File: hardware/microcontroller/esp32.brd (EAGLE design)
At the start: 108 x 93.9 mm, 20 parts, among them IC1 ESP32-WROOM-32U, IC2 AMS1117-1.5

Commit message: ESP32 Schematic clean-up
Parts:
- removed J3: (no value), con-amp:10X06MTA
- added UPLOAD_PROGRAMME: (no value), con-amp:1X6MTA
- GSM: device con-amp:1X4MTA -> con-amp:1X5MTA
- RFID: device con-amp:10X08MTA -> con-amp:1X8MTA
- moved GSM 81.0 mm to (-12.7, -34.3), turned to 0 degrees
- moved RFID 34.3 mm to (-6.35, -19.1), turned to 0 degrees
- moved POWER 17.0 mm to (74.9, 9.62)
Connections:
- new net GSM_VCC: GSM.5, GSM_VCC.1
- net GND: now also GSM.4, UPLOAD_PROGRAMME.6; no longer GSM.3, J3.6
- net GSM_RESET: now also GSM.3; no longer GSM.4, GSM_VCC.1
- net RX: now also UPLOAD_PROGRAMME.2; no longer J3.2
- net TX: now also UPLOAD_PROGRAMME.3; no longer J3.3
- net VCC: now also UPLOAD_PROGRAMME.4; no longer J3.4
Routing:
- net GSM_RX: track 137.5 -> 26.3 mm
- net GND: track 250.8 -> 285.3 mm
- net ADE_SCK: track 19.4 -> 41.6 mm
- net VCC: track 74.6 -> 83.3 mm
- net TX: track 34.3 -> 42.0 mm
- net RFID_RST: track 30.1 -> 22.5 mm
- net GSM_TX: track 181.2 -> 175.3 mm
- net GSM_RESET: track 45.7 -> 40.5 mm
- net 3V3: track 85.6 -> 81.4 mm
- net RFID_CS: track 82.4 -> 79.8 mm
- net RX: track 21.8 -> 23.4 mm
- net RFID_SCK: track 38.6 -> 37.3 mm

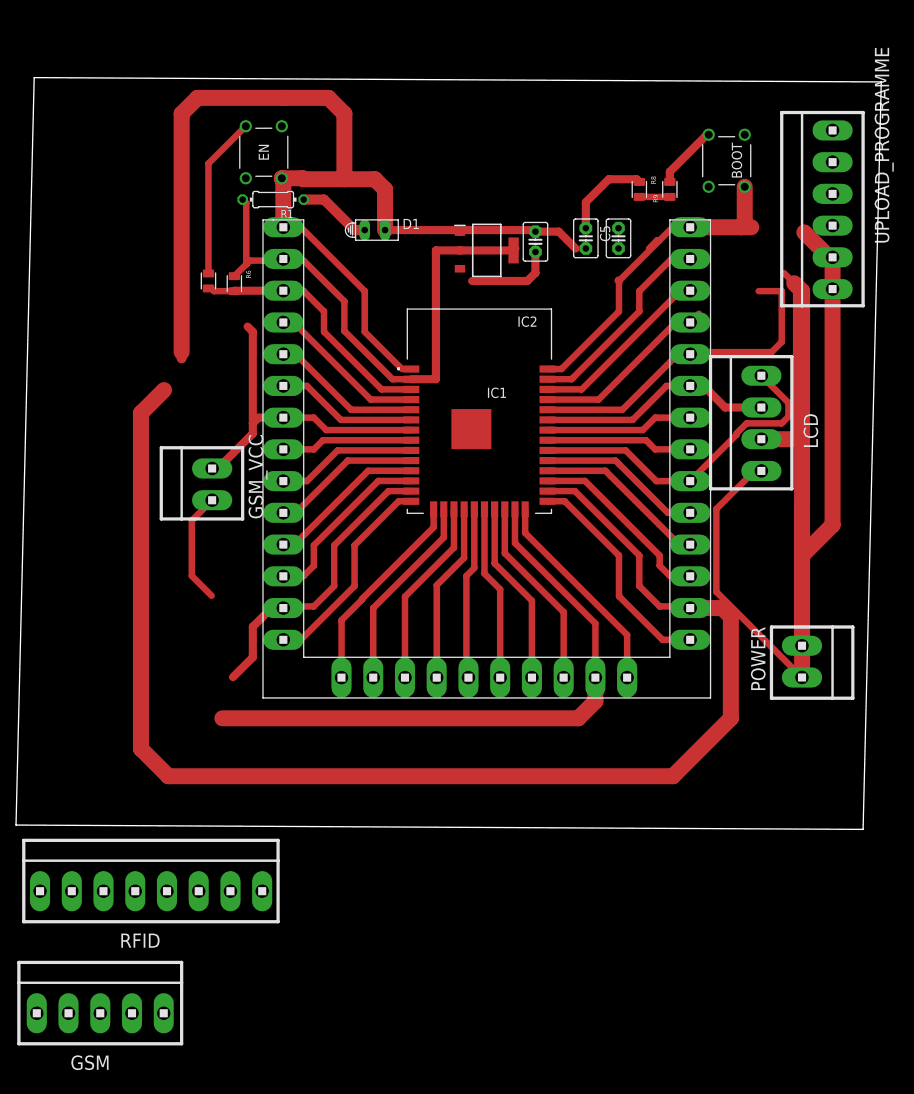
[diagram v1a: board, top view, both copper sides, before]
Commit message: ESP32 Schematic and Board Cleanup
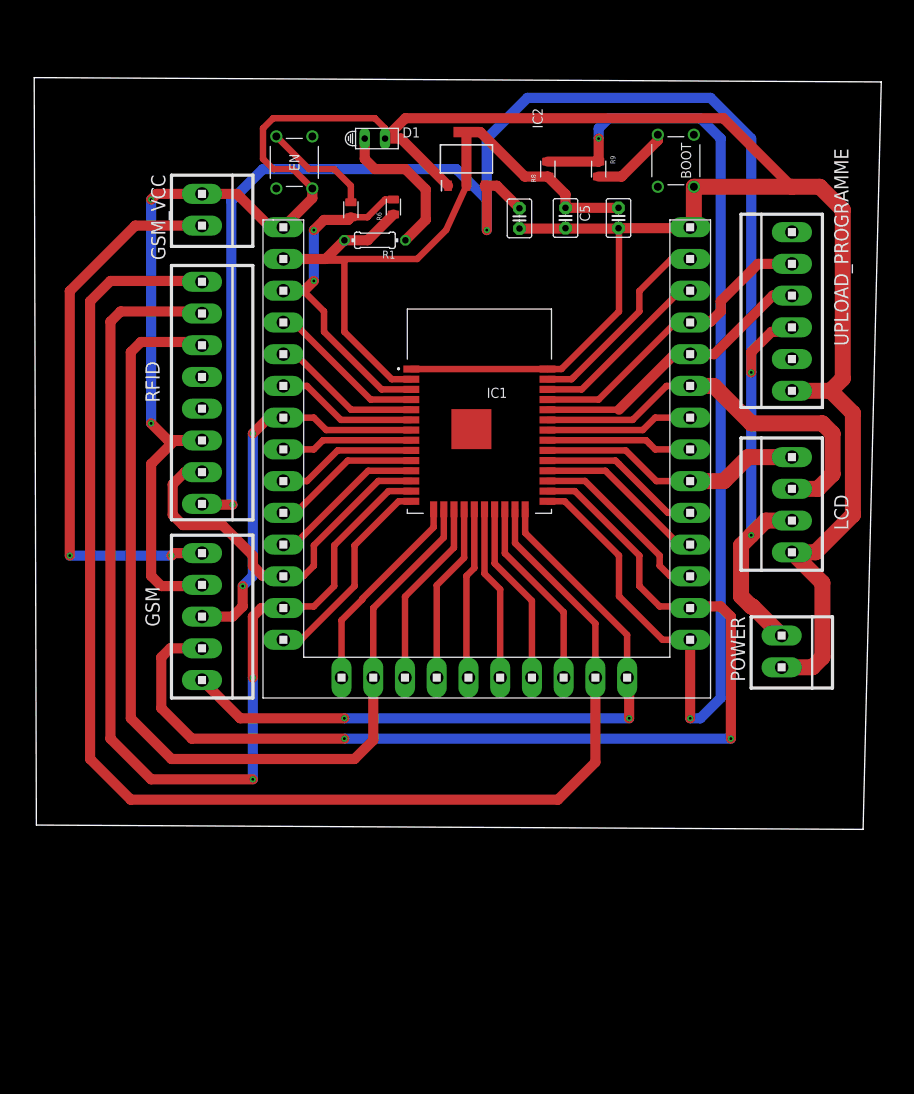
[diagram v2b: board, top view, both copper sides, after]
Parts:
- moved RFID 62.6 mm to (0.00, 43.2), turned to 270 degrees
- moved GSM 51.1 mm to (0.00, 15.2), turned to 270 degrees
- moved GSM_VCC 34.3 mm to (0.00, 66.0), turned to 270 degrees
- moved R6 22.0 mm to (23.9, 66.4), turned to 90 degrees
- moved R7 19.9 mm to (18.6, 66.0)
- moved UPLOAD_PROGRAMME 13.7 mm to (73.7, 53.3)
- moved R1 13.7 mm to (21.6, 62.2)
- moved IC2 11.7 mm to (33.0, 72.4), turned to 90 degrees
- moved R8 11.7 mm to (43.2, 71.1), turned to 90 degrees
- moved D1 11.4 mm to (21.6, 74.9)
- moved LCD 10.9 mm to (73.7, 29.2)
- moved R9 9.25 mm to (49.5, 71.1), turned to 270 degrees
- moved BOOT 6.35 mm to (61.4, 75.4)
- moved EN 4.02 mm to (13.8, 75.2)
- moved C5 3.59 mm to (45.4, 65.0)
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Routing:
- net VCC: track 83.3 -> 216.3 mm, vias 0 -> 4
- net BOOT: track 31.8 -> 139.8 mm, vias 0 -> 2
- net RFID_SCK: track 37.3 -> 133.9 mm, vias 0 -> 2
- net RFID_MOSI: track 24.7 -> 121.1 mm
- net RFID_CS: track 79.8 -> 175.1 mm
- net GSM_VCC: track 0.00 -> 69.6 mm, vias 0 -> 2
- net GSM_RX: track 26.3 -> 88.3 mm, vias 0 -> 2
- net GND: track 285.3 -> 345.9 mm, vias 0 -> 2
- net GSM_TX: track 175.3 -> 131.6 mm, vias 0 -> 2
- net RFID_RST: track 22.5 -> 48.3 mm
- net ADE_SDA_CF2: track 28.5 -> 50.7 mm
- net 3V3: track 81.4 -> 103.6 mm
- net RX: track 23.4 -> 38.3 mm
- net EN: track 38.7 -> 51.8 mm, vias 0 -> 2
- net N$41: track 9.20 -> 19.1 mm
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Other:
- board size 108 x 93.9 mm -> 105.8 x 93.9 mm

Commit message: ESP32_design
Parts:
- moved IC2 45.8 mm to (1.27, 39.4)
- moved R8 45.7 mm to (-2.54, 71.1)
- moved C1 39.7 mm to (79.0, 70.0)
- moved D1 33.0 mm to (-11.4, 74.9), turned to 180 degrees
- moved C5 29.6 mm to (74.6, 70.1)
- moved C2 29.0 mm to (78.7, 76.4)
- moved R6 26.2 mm to (1.04, 53.7)
- moved IC1 25.5 mm to (36.8, 66.0)
- moved R1 23.1 mm to (-1.16, 66.2), turned to 0 degrees
- moved R9 22.9 mm to (71.8, 76.2)
- moved R7 18.9 mm to (0.81, 59.7)
- moved GSM_VCC 11.5 mm to (-11.4, 67.3)
- moved RFID 11.5 mm to (-11.4, 44.5)
- moved GSM 11.4 mm to (-11.4, 15.2)
- moved BOOT 3.81 mm to (65.2, 75.4)
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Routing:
- net RFID_CS: track 175.1 -> 49.5 mm
- net GND: track 345.9 -> 226.4 mm, vias 2 -> 0
- net VCC: track 216.3 -> 108.1 mm, vias 4 -> 0
- net BOOT: track 139.8 -> 49.8 mm, vias 2 -> 0
- net RFID_SCK: track 133.9 -> 50.3 mm, vias 2 -> 0
- net RFID_MOSI: track 121.1 -> 51.1 mm
- net GSM_VCC: track 69.6 -> 0.00 mm, vias 2 -> 0
- net 3V3: track 103.6 -> 61.3 mm
- net GSM_RX: track 88.3 -> 122.0 mm, vias 2 -> 0
- net 18: track 22.4 -> 53.5 mm
- net GSM_TX: track 131.6 -> 162.4 mm, vias 2 -> 0
- net 11: track 19.8 -> 46.6 mm
- net GSM_RESET: track 49.0 -> 75.5 mm, vias 2 -> 0
- net 17: track 23.6 -> 50.0 mm
- net 15: track 25.8 -> 52.2 mm
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
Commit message: ESP32_Final Design
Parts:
- turned R6 to 270 degrees
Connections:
- removed net REID_MISO: RFID.5
- net RFID_MISO: now also RFID.5
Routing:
- net BOOT: track 49.8 -> 191.6 mm, vias 0 -> 3
- net VCC: track 108.1 -> 243.1 mm, vias 0 -> 2
- net RFID_MOSI: track 51.1 -> 154.7 mm, vias 0 -> 2
- net GND: track 226.4 -> 325.9 mm, vias 0 -> 2
- net RFID_CS: track 49.5 -> 140.1 mm, vias 0 -> 3
- net 3V3: track 61.3 -> 150.9 mm, vias 0 -> 6
- net RFID_SCK: track 50.3 -> 103.3 mm, vias 0 -> 2
- net GSM_VCC: track 0.00 -> 50.8 mm, vias 0 -> 2
- net RFID_MISO: track 52.3 -> 102.8 mm, vias 0 -> 2
- net RFID_RST: track 48.9 -> 81.8 mm, vias 0 -> 2
- net N$23: track 0.00 -> 20.6 mm, vias 0 -> 2
- net EN: track 28.7 -> 47.8 mm

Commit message: files change
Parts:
- moved IC1 3.57 mm to (38.7, 69.1)
- turned R6 to 90 degrees
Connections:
- new net REID_MISO: RFID.5
- net RFID_MISO: no longer RFID.5
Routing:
- net BOOT: track 191.6 -> 52.1 mm, vias 3 -> 0
- net VCC: track 243.1 -> 108.1 mm, vias 2 -> 0
- net GND: track 325.9 -> 208.3 mm, vias 2 -> 0
- net RFID_MOSI: track 154.7 -> 54.9 mm, vias 2 -> 0
- net RFID_CS: track 140.1 -> 51.8 mm, vias 3 -> 0
- net 3V3: track 150.9 -> 64.4 mm, vias 6 -> 0
- net GSM_VCC: track 50.8 -> 0.00 mm, vias 2 -> 0
- net RFID_SCK: track 103.3 -> 53.4 mm, vias 2 -> 0
- net RFID_MISO: track 102.8 -> 56.1 mm, vias 2 -> 0
- net RFID_RST: track 81.8 -> 52.0 mm, vias 2 -> 0
- net N$23: track 20.6 -> 0.00 mm, vias 2 -> 0
- net EN: track 47.8 -> 31.8 mm
- net 18: track 53.5 -> 57.3 mm
- net 22: track 48.5 -> 52.3 mm
- net 20: track 46.7 -> 50.5 mm
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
